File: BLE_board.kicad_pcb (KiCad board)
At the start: 4 copper layers, 0 parts

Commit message: First basic design
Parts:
- added AE1: PCB Antenna, RF_Antenna:Texas_SWRA117D_2.4GHz_Right, F.Cu at (138.7, 75.3)
- added C1: 4.7u, Capacitor_SMD:C_0402_1005Metric, F.Cu at (103.6, 56.1)
- added C10: 1p, Capacitor_SMD:C_0402_1005Metric, F.Cu at (136.4, 75.0)
- added C11: 4.7p, Capacitor_SMD:C_0402_1005Metric, F.Cu at (136.9, 81.4)
- added C12: 2.2n, Capacitor_SMD:C_0402_1005Metric, F.Cu at (136.9, 80.4)
- added C13: 4.7u, Capacitor_SMD:C_0402_1005Metric, F.Cu at (103.6, 60.1)
- added C14: 100n, Capacitor_SMD:C_0402_1005Metric, F.Cu at (103.6, 62.0)
- added C15: 1u, Capacitor_SMD:C_0402_1005Metric, F.Cu at (103.6, 64.0)
- added C16: 10n, Capacitor_SMD:C_0402_1005Metric, F.Cu at (103.6, 66.0)
- added C17: 10n, Capacitor_SMD:C_0402_1005Metric, F.Cu at (109.1, 77.6)
- added C18: 100n, Capacitor_SMD:C_0402_1005Metric, F.Cu at (114.6, 81.4)
- added C19: 100n, Capacitor_SMD:C_0402_1005Metric, F.Cu at (109.0, 76.2)
- added C2: 100n, Capacitor_SMD:C_0402_1005Metric, F.Cu at (103.6, 58.1)
- added C20: 4.7u, Capacitor_SMD:C_0402_1005Metric, F.Cu at (109.0, 75.1)
- added C3: C_Small, Capacitor_SMD:C_0402_1005Metric, F.Cu at (128.8, 83.2)
- added C4: C_Small, Capacitor_SMD:C_0402_1005Metric, F.Cu at (134.1, 83.2)
- added C5: 33n, Capacitor_SMD:C_0402_1005Metric, F.Cu at (128.7, 75.0)
- added C6: 4.7u, Capacitor_SMD:C_0402_1005Metric, F.Cu at (130.7, 73.0)
- added C7: 10n, Capacitor_SMD:C_0402_1005Metric, F.Cu at (130.7, 74.0)
- added C8: 1n, Capacitor_SMD:C_0402_1005Metric, F.Cu at (130.7, 75.0)
- added C9: 1.5p, Capacitor_SMD:C_0402_1005Metric, F.Cu at (136.4, 77.0)
- added F1: 500mA, Capacitor_SMD:C_1206_3216Metric, F.Cu at (108.9, 72.6)
- added FB1: 33ohm @ 100MHz, Inductor_SMD:L_0402_1005Metric, F.Cu at (107.1, 76.5)
- added J1: USB_C_Receptacle_USB2.0_14P, Connector_USB:USB_C_Receptacle_XKB_U262-16XN-4BVC11, F.Cu at (103.5, 83.7)
- added L1: 8.2n, Capacitor_SMD:C_0402_1005Metric, F.Cu at (134.4, 78.8)
- added L2: 2.7n, Capacitor_SMD:C_0402_1005Metric, F.Cu at (135.4, 79.9)
- added L3: 3.9n, Capacitor_SMD:C_0402_1005Metric, F.Cu at (135.9, 78.4)
- added R1: 22k, Capacitor_SMD:C_0402_1005Metric, F.Cu at (132.8, 75.1)
- added R2: 5k1, Resistor_SMD:R_0402_1005Metric, F.Cu at (111.1, 86.3)
- added R3: 5k1, Resistor_SMD:R_0402_1005Metric, F.Cu at (110.4, 81.9)
- added U1: STM32F042G6U6, Package_DFN_QFN:QFN-28_4x4mm_P0.5mm, F.Cu at (121.1, 78.5)
- added U2: nRF24L01P, Package_DFN_QFN:QFN-20-1EP_4x4mm_P0.5mm_EP2.5x2.5mm, F.Cu at (130.2, 78.7)
- added U3: USBLC6-2P6, Package_TO_SOT_SMD:SOT-666, F.Cu at (114.5, 84.2)
- added Y1: Crystal_GND24_Small, Crystal:Crystal_SMD_3225-4Pin_3.2x2.5mm, F.Cu at (131.4, 83.3)
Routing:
- net GND: track 0.00 -> 24.3 mm, vias 0 -> 11
- net +3V3: track 0.00 -> 12.4 mm, vias 0 -> 2
- net /RF Module/XC2: track 0.00 -> 6.32 mm
- net /RF Module/VDD_PA: track 0.00 -> 5.48 mm
- net /RF Module/XC1: track 0.00 -> 4.03 mm
- net /RF Module/ANT2: track 0.00 -> 3.37 mm
- net /RF Module/ANT1: track 0.00 -> 3.32 mm
- net Net-(AE1-A): track 0.00 -> 3.31 mm
- net Net-(U2-IREF): track 0.00 -> 2.04 mm
- net Net-(U2-DVDD): track 0.00 -> 1.97 mm
- net Net-(C9-Pad1): track 0.00 -> 0.96 mm
- added copper zone on In2.Cu, net +3V3
- added copper zone on F.Cu, net GND
- added copper zone on In1.Cu, net GND
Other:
- board outline added: 43.9 x 19.1 mm

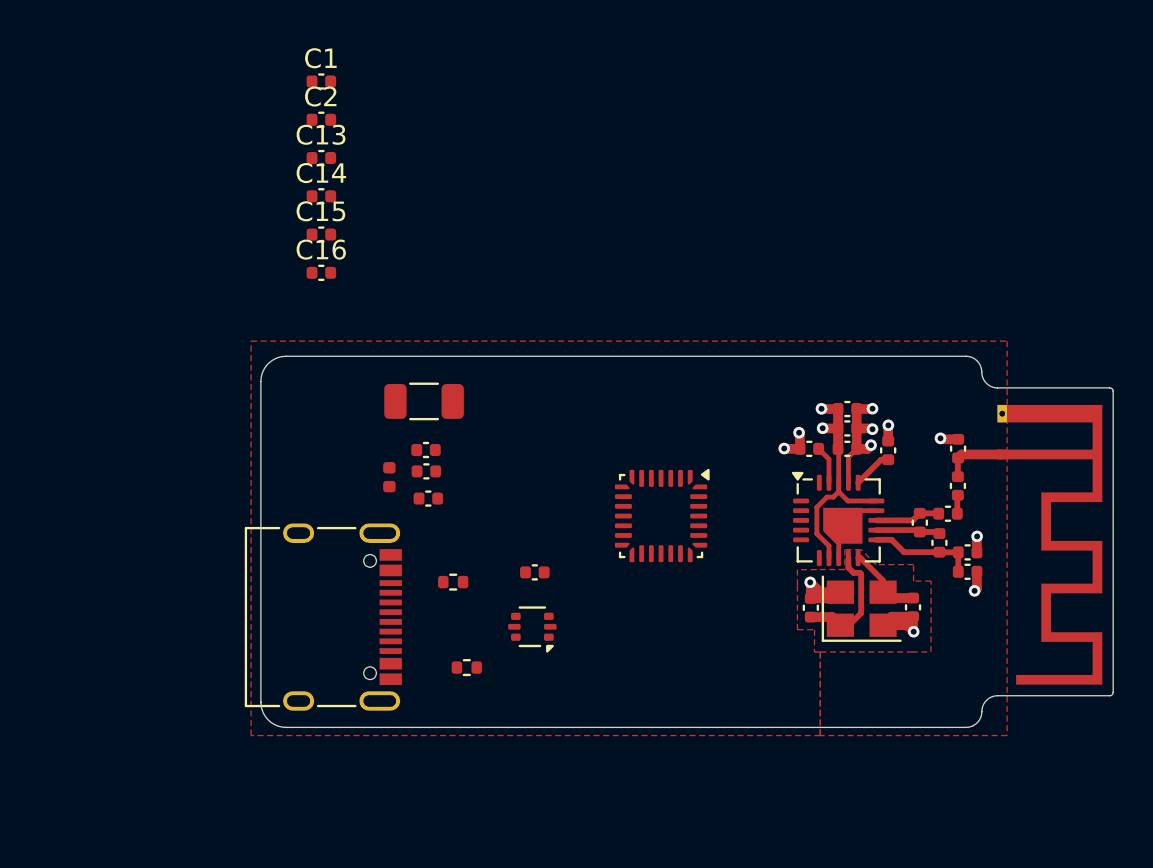
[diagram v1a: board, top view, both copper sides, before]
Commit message: Redesigned power supply. First board draft
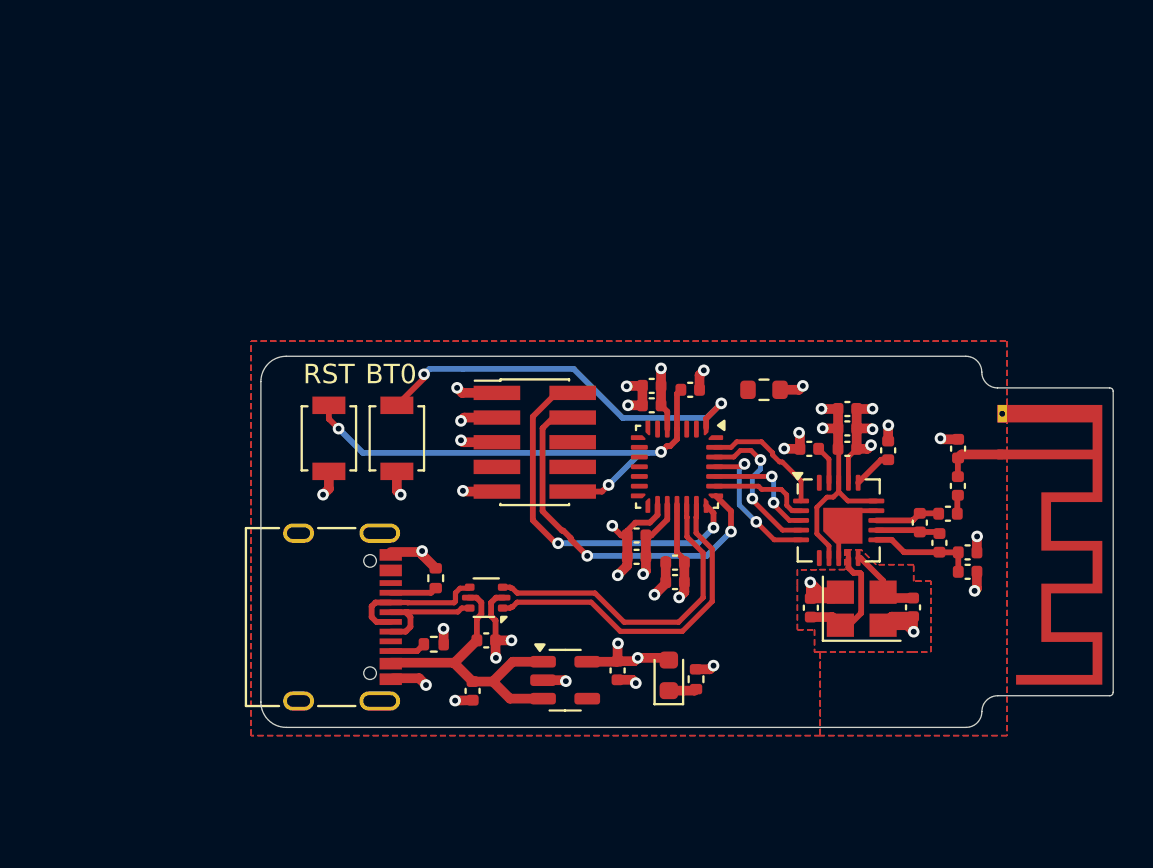
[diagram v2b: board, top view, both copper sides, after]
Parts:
- removed C20: 4.7u, Capacitor_SMD:C_0402_1005Metric
- removed F1: 500mA, Capacitor_SMD:C_1206_3216Metric
- removed FB1: 33ohm @ 100MHz, Inductor_SMD:L_0402_1005Metric
- added C21: 0.1u, Capacitor_SMD:C_0402_1005Metric, F.Cu at (122.6, 72.0)
- added D1: Power, LED_SMD:LED_0603_1608Metric, F.Cu at (121.5, 86.7)
- added J2: SWD, Connector_PinHeader_1.27mm:PinHeader_2x05_P1.27mm_Vertical_SMD, F.Cu at (114.6, 74.7)
- added R4: 10k, Resistor_SMD:R_0603_1608Metric, F.Cu at (126.4, 72.0)
- added R5: 2k2, Resistor_SMD:R_0402_1005Metric, F.Cu at (122.9, 86.9)
- added SW1: NRST, Button_Switch_SMD:SW_SPST_B3U-1000P, F.Cu at (104.0, 74.5)
- added SW2: BOOT0, Button_Switch_SMD:SW_SPST_B3U-1000P, F.Cu at (107.5, 74.5)
- added U4: MIC5365-3.3YD5, Package_TO_SOT_SMD:SOT-23-5, F.Cu at (116.2, 86.9)
- C17: value 10n -> 1u
- C19: value 100n -> 1u
- moved C1 29.4 mm to (119.8, 80.6), turned to 180 degrees
- moved C13 28.4 mm to (121.8, 81.9), turned to 180 degrees
- moved C2 26.9 mm to (119.8, 79.5), turned to 180 degrees
- moved C14 26.2 mm to (121.8, 80.9), turned to 180 degrees
- moved C15 18.7 mm to (120.6, 71.8), turned to 180 degrees
- moved C16 18.3 mm to (120.6, 72.8), turned to 180 degrees
- moved C19 14.2 mm to (118.9, 86.4), turned to -90 degrees
- moved C17 10.2 mm to (111.4, 87.5), turned to -90 degrees
- moved C18 4.30 mm to (112.1, 84.9)
- moved U3 2.81 mm to (112.1, 82.7)
- moved U1 2.67 mm to (121.9, 76.0)
- moved R2 2.08 mm to (109.4, 85.1)
- moved R3 0.92 mm to (109.5, 81.7), turned to 90 degrees
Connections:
- C19 pad 1: Net-(C19-Pad1) -> +3V3
- U1 pad 21: unconnected-(U1-PA13-Pad21) -> /MCU Module/SWDIO
- U1 pad 22: unconnected-(U1-PA14-Pad22) -> /MCU Module/SWCLK
- U1 pad 4: unconnected-(U1-NRST-Pad4) -> /MCU Module/NRST
- U2 pad 21: (no net) -> GND
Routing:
- net GND: track 24.3 -> 61.0 mm, vias 11 -> 31
- net /MCU Module/NRST: track 0.00 -> 26.9 mm, vias 0 -> 3
- net +3V3: track 12.4 -> 33.7 mm, vias 2 -> 9
- net Net-(U1-PB8): track 0.00 -> 20.5 mm, vias 0 -> 2
- net /MCU Module/SWCLK: track 0.00 -> 19.4 mm, vias 0 -> 2
- net /MCU Module/SWDIO: track 0.00 -> 19.3 mm, vias 0 -> 2
- net /MCU Module/USB_D+: track 0.00 -> 17.5 mm
- net /MCU Module/USB_D-: track 0.00 -> 16.7 mm
- net /USB and Power/+VBUS: track 0.00 -> 16.1 mm
- net /MCU Module/SPI_MOSI: track 0.00 -> 8.09 mm, vias 0 -> 2
- net /MCU Module/SPI_MISO: track 0.00 -> 7.75 mm, vias 0 -> 2
- net /USB and Power/USB_CONN_D-: track 0.00 -> 7.37 mm
- net /USB and Power/USB_CONN_D+: track 0.00 -> 6.89 mm
- net /MCU Module/RF_CE: track 0.00 -> 6.51 mm
- net /MCU Module/SPI_SCK: track 0.00 -> 6.18 mm, vias 0 -> 2
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- added copper zone on B.Cu, net GND
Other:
- board text added: "BT0"
- board text added: "RST"

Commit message: First routed board
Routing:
- net /MCU Module/RF_IRQ: track 0.00 -> 12.2 mm, vias 0 -> 2
- net GND: track 61.0 -> 72.0 mm, vias 31 -> 49
- net /USB and Power/+VBUS: track 16.1 -> 22.5 mm, vias 0 -> 2
- net Net-(U1-PB8): track 20.5 -> 22.2 mm

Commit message: BOM assigned
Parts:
- removed U4: MIC5365-3.3YD5, Package_TO_SOT_SMD:SOT-23-5
- added U5: MIC5365-3.3YC5, Package_TO_SOT_SMD:SOT-353_SC-70-5, F.Cu at (114.8, 87.4)
- moved R5 2.14 mm to (120.8, 87.5)
- moved D1 2.14 mm to (119.4, 87.2)
- moved C19 2.00 mm to (117.0, 87.3)
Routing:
- net /USB and Power/+VBUS: track 22.5 -> 21.0 mm
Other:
- board text added: "PWR"

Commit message: Minor changes
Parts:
- C21: value 0.1u -> 100n
- C3, C4: value C_Small -> 12p
- J2: footprint Connector_PinHeader_1.27mm:PinHeader_2x05_P1.27mm_Vertical_SMD -> Custom_Connectors:PinHeader_2x05_P1.27mm_Vertical_SMD_w_fiducials
- Y1: value Crystal_GND24_Small -> 16MHz
- turned J2 to -90 degrees
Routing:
- net /MCU Module/SWDIO: track 19.3 -> 11.1 mm
- net /MCU Module/SWCLK: track 19.4 -> 14.7 mm
- net Net-(U1-PB8): track 22.2 -> 20.5 mm
- net +3V3: track 33.4 -> 32.6 mm
- net /MCU Module/NRST: track 26.9 -> 26.5 mm, vias 3 -> 2
- net GND: track 71.7 -> 72.1 mm, vias 49 -> 48
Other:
- board text added: "BLE+USB Test v0.1"
- board text added: "JLCJLCJLCJLC"

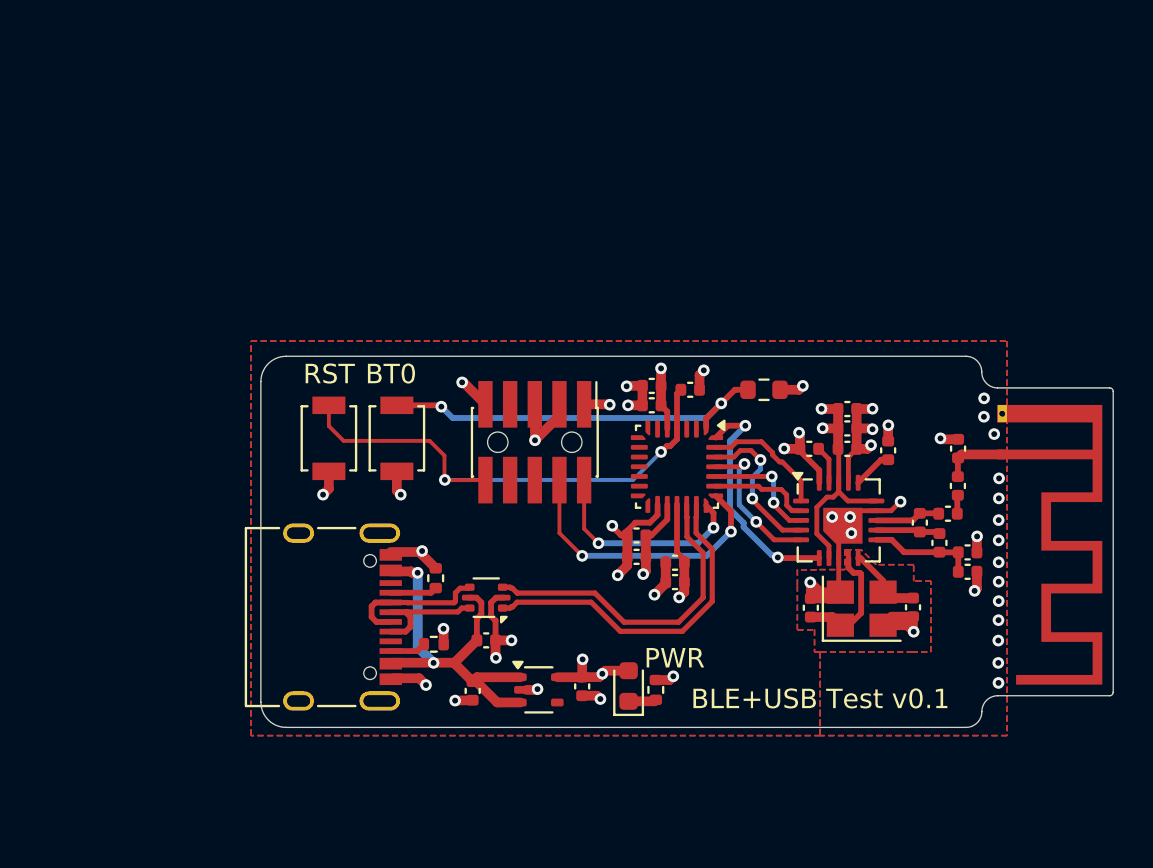
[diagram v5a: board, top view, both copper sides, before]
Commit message: Larger dimensions. Include mounting holes. Better antenna feed alignment
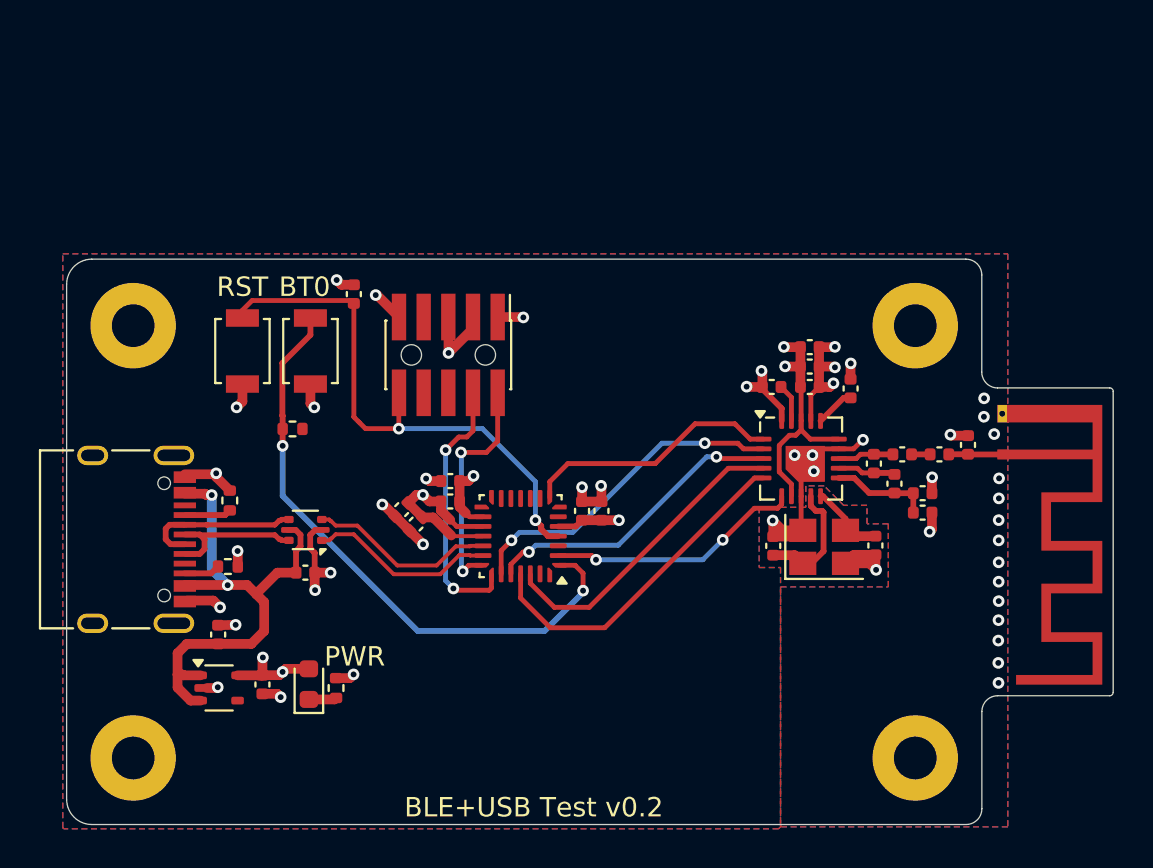
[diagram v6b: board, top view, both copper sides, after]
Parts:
- added H101: MountingHole_Pad, MountingHole:MountingHole_2.2mm_M2_Pad, F.Cu at (93.9, 68.7)
- added H102: MountingHole_Pad, MountingHole:MountingHole_2.2mm_M2_Pad, F.Cu at (134.2, 68.7)
- added H103: MountingHole_Pad, MountingHole:MountingHole_2.2mm_M2_Pad, F.Cu at (134.2, 91.0)
- added H104: MountingHole_Pad, MountingHole:MountingHole_2.2mm_M2_Pad, F.Cu at (93.9, 91.0)
- R4: footprint Resistor_SMD:R_0603_1608Metric -> Resistor_SMD:R_0402_1005Metric
- moved R4 24.4 mm to (102.1, 74.0)
- moved C21 18.0 mm to (105.3, 67.1), turned to -90 degrees
- moved C19 16.5 mm to (100.6, 87.2)
- moved D1 16.5 mm to (103.0, 87.2)
- moved U5 16.5 mm to (98.3, 87.3)
- moved R5 16.5 mm to (104.4, 87.4)
- moved C13 14.6 mm to (107.7, 78.2), turned to -135 degrees
- moved C14 13.5 mm to (108.5, 78.9), turned to -135 degrees
- moved C17 13.4 mm to (98.3, 84.6), turned to 90 degrees
- moved R2 11.3 mm to (98.8, 81.1)
- moved J1 11.3 mm to (92.9, 79.7)
- moved R3 11.3 mm to (98.9, 77.7)
- moved C1 10.4 mm to (110.2, 76.7), turned to 0 degrees
- moved C18 9.94 mm to (102.8, 81.4)
- moved U3 9.94 mm to (102.8, 79.2)
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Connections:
- net Net-(U1-PB8) renamed /MCU Module/boot0
- C21 pad 1: GND -> /MCU Module/NRST
- C21 pad 2: /MCU Module/NRST -> GND
- U1 pad 2: unconnected-(U1-PF0-Pad2) -> /MCU Module/RF_IRQ
- U1 pad 27: /MCU Module/RF_CE -> unconnected-(U1-PB6-Pad27)
- U1 pad 28: /MCU Module/RF_IRQ -> unconnected-(U1-PB7-Pad28)
- U1 pad 8: unconnected-(U1-PA2-Pad8) -> /MCU Module/RF_CE
- U2 pad 21: GND -> (no net)
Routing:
- net /MCU Module/SPI_CS: track 5.29 -> 17.1 mm, vias 0 -> 2
- net /MCU Module/boot0: track 20.5 -> 31.3 mm
- net /MCU Module/SPI_MISO: track 7.75 -> 17.6 mm, vias 2 -> 0
- net /MCU Module/SPI_SCK: track 6.18 -> 15.8 mm
- net /MCU Module/SPI_MOSI: track 8.09 -> 16.0 mm, vias 2 -> 0
- net /MCU Module/USB_D+: track 17.5 -> 9.69 mm
- net /MCU Module/USB_D-: track 16.7 -> 9.69 mm
- net /MCU Module/RF_CE: track 6.51 -> 13.4 mm
- net /USB and Power/+VBUS: track 21.0 -> 27.1 mm
- net GND: track 72.1 -> 66.4 mm, vias 48 -> 46
- net /MCU Module/NRST: track 26.5 -> 29.5 mm, vias 2 -> 3
- net +3V3: track 32.6 -> 33.7 mm
- net /MCU Module/RF_IRQ: track 12.2 -> 13.2 mm
- net /MCU Module/SWCLK: track 14.7 -> 13.8 mm
- net /USB and Power/USB_CONN_D-: track 7.37 -> 8.26 mm
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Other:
- board size 43.9 x 19.1 mm -> 53.9 x 29.1 mm
- board text added: "BLE+USB Test v0.2"
- board text removed: "BLE+USB Test v0.1"

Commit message: Add signaling LEDs
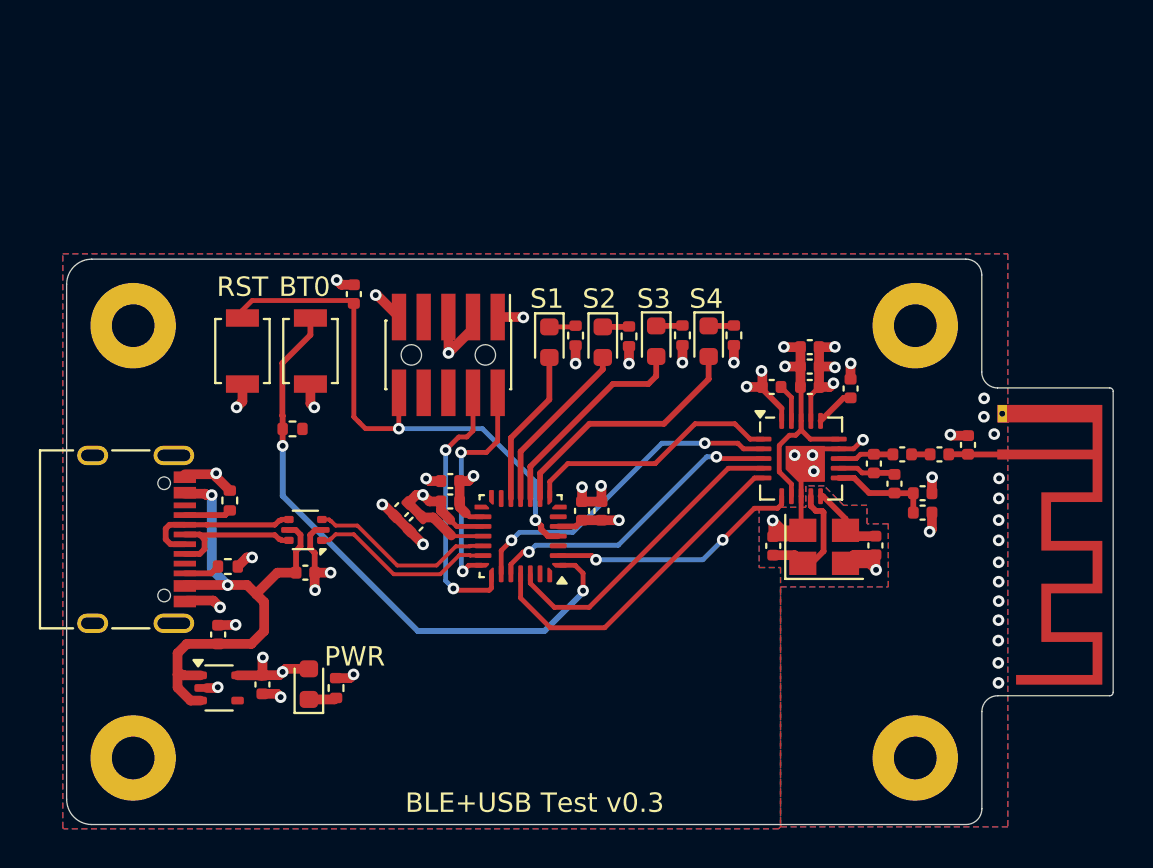
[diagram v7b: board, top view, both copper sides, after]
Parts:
- added D301: SIG1, LED_SMD:LED_0603_1608Metric, F.Cu at (115.3, 69.5)
- added D302: SIG2, LED_SMD:LED_0603_1608Metric, F.Cu at (118.1, 69.5)
- added D303: SIG3, LED_SMD:LED_0603_1608Metric, F.Cu at (120.8, 69.5)
- added D304: SIG4, LED_SMD:LED_0603_1608Metric, F.Cu at (123.5, 69.5)
- added R301: 2k2, Resistor_SMD:R_0402_1005Metric, F.Cu at (116.7, 69.2)
- added R302: 2k2, Resistor_SMD:R_0402_1005Metric, F.Cu at (119.5, 69.2)
- added R303: 2k2, Resistor_SMD:R_0402_1005Metric, F.Cu at (122.2, 69.2)
- added R304: 2k2, Resistor_SMD:R_0402_1005Metric, F.Cu at (124.8, 69.2)
- turned C21 to 90 degrees
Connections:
- U1 pad 10: unconnected-(U1-PA4-Pad10) -> /MCU Module/SIG3
- U1 pad 11: unconnected-(U1-PA5-Pad11) -> /MCU Module/SIG2
- U1 pad 12: unconnected-(U1-PA6-Pad12) -> /MCU Module/SIG1
- U1 pad 9: unconnected-(U1-PA3-Pad9) -> /MCU Module/SIG4
- U2 pad 21: (no net) -> GND
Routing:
- net /MCU Module/SIG4: track 0.00 -> 13.2 mm
- net /MCU Module/SIG3: track 0.00 -> 11.1 mm
- net /MCU Module/SIG2: track 0.00 -> 9.01 mm
- net /MCU Module/SIG1: track 0.00 -> 8.08 mm
- net GND: track 66.4 -> 71.2 mm, vias 46 -> 51
- net Net-(D301-K): track 0.00 -> 1.38 mm
- net Net-(D303-K): track 0.00 -> 1.36 mm
- net Net-(D302-K): track 0.00 -> 1.36 mm
- net Net-(D304-K): track 0.00 -> 1.31 mm
- net /MCU Module/NRST: track 29.5 -> 28.5 mm, vias 3 -> 2
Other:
- board text added: "BLE+USB Test v0.3"
- board text added: "S1"
- board text added: "S2"
- board text added: "S3"
- board text added: "S4"
- board text removed: "BLE+USB Test v0.2"
